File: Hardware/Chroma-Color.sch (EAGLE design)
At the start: 92 parts, among them J1 15-91-1102, J2 87832-6422, J3 1775470-6, J4 D2514-6V0C-AR-WD, J7 26-64-4040, U1 EP4CE6E22C8N, U2 ADP3338AKCZ-3.3-RL, U3 ADP3338AKCZ-2.5-RL, U4 NCV565ST12T3G, U5 M25P40-VMN6TPBCT, X1 ASDMB-50.000MHZ-LC-T

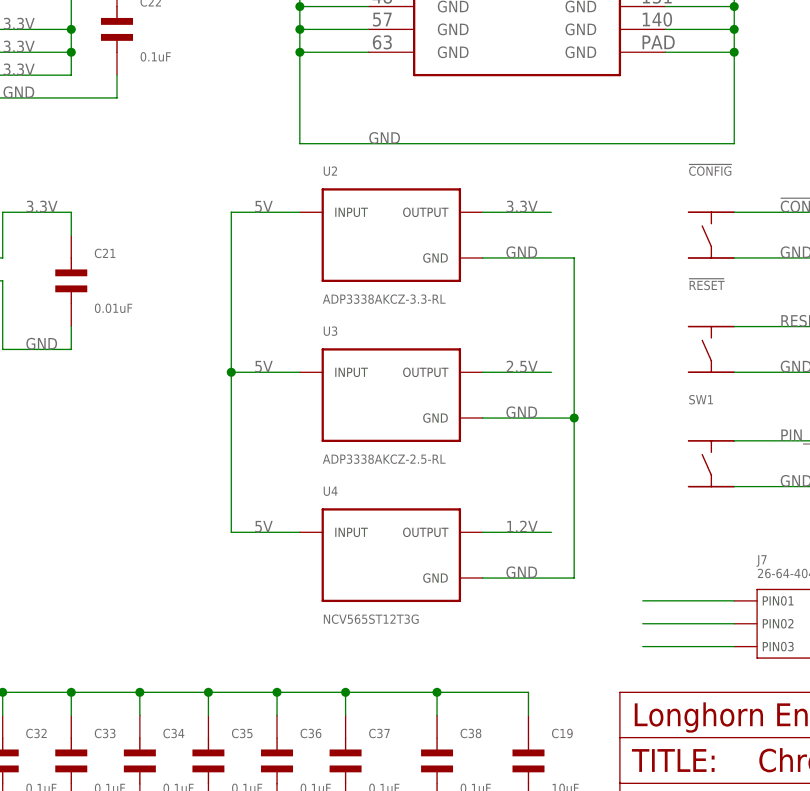
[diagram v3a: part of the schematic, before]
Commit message: Fixed voltage regulators to use newer library
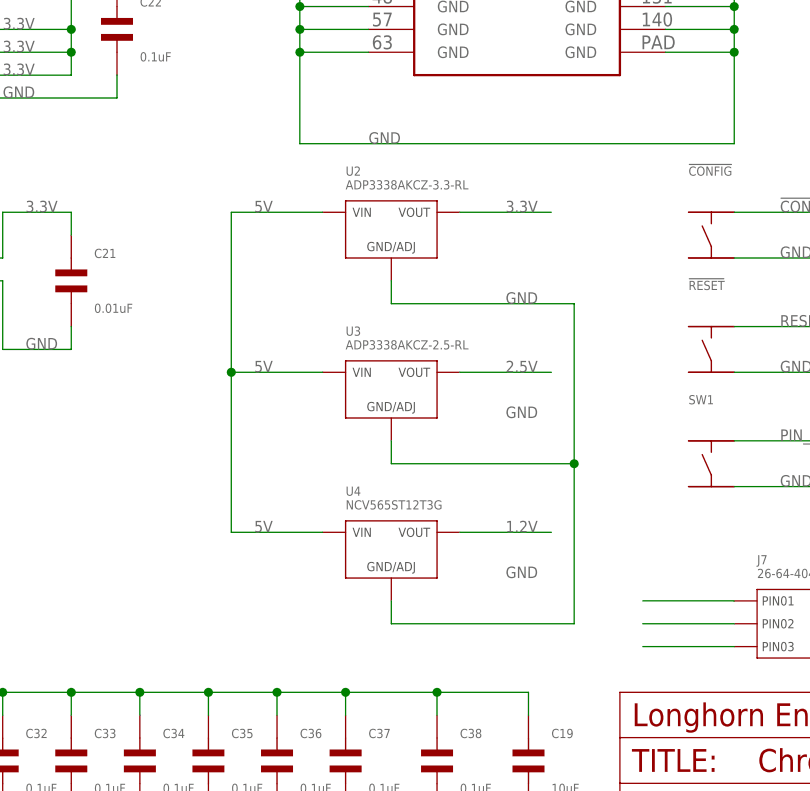
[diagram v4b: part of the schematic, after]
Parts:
- U2: device PP_PowerIC:ADP3338AKCZ-3.3-RL -> PP_PowerIC:LINEAR_VOTLAGE_REGULATORS_ADP3338
- U3: device PP_PowerIC:ADP3338AKCZ-2.5-RL -> PP_PowerIC:LINEAR_VOTLAGE_REGULATORS_ADP3338
- U4: device PP_PowerIC:NCV565ST12T3G -> PP_PowerIC:LINEAR_VOTLAGE_REGULATORS_NCV565ST12T3G
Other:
- moved on the sheet: U2, U3, U4

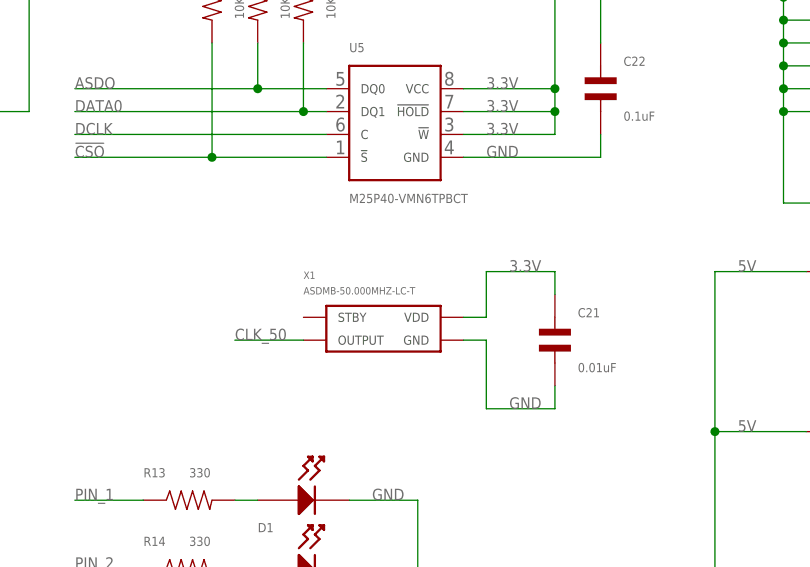
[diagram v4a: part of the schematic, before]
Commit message: Updated to latest library style.
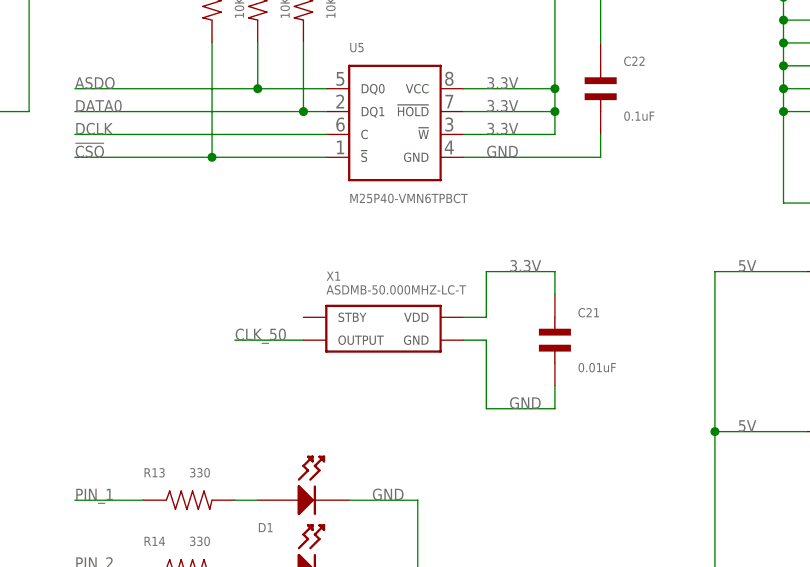
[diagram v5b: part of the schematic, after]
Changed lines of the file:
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@@
 <grid distance="0.1" unitdist="inch" unit="inch" style="lines" multiple="1" display="no" altdistance="0.01" altunitdist="inch" altunit="inch"/>
 <layers>
-<layer number="1" name="Top" color="14" fill="1" visible="yes" active="no"/>
-<layer number="2" name="Route2" color="12" fill="1" visible="yes" active="no"/>
-<layer number="3" name="Route3" color="4" fill="3" visible="yes" active="no"/>
-<layer number="4" name="Route4" color="1" fill="4" visible="yes" active="no"/>
-<layer number="5" name="Route5" color="4" fill="4" visible="yes" active="no"/>
-<layer number="6" name="Route6" color="1" fill="8" visible="yes" active="no"/>
-<layer number="7" name="Route7" color="4" fill="8" visible="yes" active="no"/>
-<layer number="8" name="Route8" color="1" fill="2" visible="yes" active="no"/>
-<layer number="9" name="Route9" color="4" fill="2" visible="yes" active="no"/>
-<layer number="10" name="Route10" color="1" fill="7" visible="yes" active="no"/>
-<layer number="11" name="Route11" color="4" fill="7" visible="yes" active="no"/>
-<layer number="12" name="Route12" color="1" fill="5" visible="yes" active="no"/>
-<layer number="13" name="Route13" color="4" fill="5" visible="yes" active="no"/>
-<layer number="14" name="Route14" color="1" fill="6" visible="yes" active="no"/>
-<layer number="15" name="Route15" color="9" fill="1" visible="yes" active="no"/>
-<layer number="16" name="Bottom" color="13" fill="1" visible="yes" active="no"/>
-<layer number="17" name="Pads" color="2" fill="1" visible="yes" active="no"/>
-<layer number="18" name="Vias" color="2" fill="1" visible="yes" active="no"/>
-<layer number="19" name="Unrouted" color="6" fill="1" visible="yes" active="no"/>
-<layer number="20" name="Dimension" color="15" fill="1" visible="yes" active="no"/>
-<layer number="21" name="tPlace" color="7" fill="1" visible="yes" active="no"/>
-<layer number="22" name="bPlace" color="7" fill="1" visible="yes" active="no"/>
-<layer number="23" name="tOrigins" color="15" fill="1" visible="yes" active="no"/>
-<layer number="24" name="bOrigins" color="15" fill="1" visible="yes" active="no"/>
-<layer number="25" name="tNames" color="7" fill="1" visible="yes" active="no"/>
-<layer number="26" name="bNames" color="7" fill="1" visible="yes" active="no"/>
-<layer number="27" name="tValues" color="7" fill="1" visible="yes" active="no"/>
-<layer number="28" name="bValues" color="7" fill="1" visible="yes" active="no"/>
+<layer number="1" name="Top" color="14" fill="1" visible="no" active="no"/>
+<layer number="2" name="Route2" color="12" fill="1" visible="no" active="no"/>
+<layer number="3" name="Route3" color="4" fill="3" visible="no" active="no"/>
+<layer number="4" name="Route4" color="1" fill="4" visible="no" active="no"/>
+<layer number="5" name="Route5" color="4" fill="4" visible="no" active="no"/>
+<layer number="6" name="Route6" color="1" fill="8" visible="no" active="no"/>
+<layer number="7" name="Route7" color="4" fill="8" visible="no" active="no"/>
+<layer number="8" name="Route8" color="1" fill="2" visible="no" active="no"/>
+<layer number="9" name="Route9" color="4" fill="2" visible="no" active="no"/>
+<layer number="10" name="Route10" color="1" fill="7" visible="no" active="no"/>
+<layer number="11" name="Route11" color="4" fill="7" visible="no" active="no"/>
+<layer number="12" name="Route12" color="1" fill="5" visible="no" active="no"/>
+<layer number="13" name="Route13" color="4" fill="5" visible="no" active="no"/>
+<layer number="14" name="Route14" color="1" fill="6" visible="no" active="no"/>
+<layer number="15" name="Route15" color="9" fill="1" visible="no" active="no"/>
+<layer number="16" name="Bottom" color="13" fill="1" visible="no" active="no"/>
+<layer number="17" name="Pads" color="2" fill="1" visible="no" active="no"/>
+<layer number="18" name="Vias" color="2" fill="1" visible="no" active="no"/>
+<layer number="19" name="Unrouted" color="6" fill="1" visible="no" active="no"/>
+<layer number="20" name="Dimension" color="15" fill="1" visible="no" active="no"/>
+<layer number="21" name="tPlace" color="7" fill="1" visible="no" active="no"/>
+<layer number="22" name="bPlace" color="7" fill="1" visible="no" active="no"/>
+<layer number="23" name="tOrigins" color="15" fill="1" visible="no" active="no"/>
+<layer number="24" name="bOrigins" color="15" fill="1" visible="no" active="no"/>
+<layer number="25" name="tNames" color="7" fill="1" visible="no" active="no"/>
+<layer number="26" name="bNames" color="7" fill="1" visible="no" active="no"/>
+<layer number="27" name="tValues" color="7" fill="1" visible="no" active="no"/>
+<layer number="28" name="bValues" color="7" fill="1" visible="no" active="no"/>
 <layer number="29" name="tStop" color="7" fill="3" visible="no" active="no"/>
 <layer number="30" name="bStop" color="7" fill="6" visible="no" active="no"/>
@@
 <layer number="35" name="tGlue" color="7" fill="4" visible="no" active="no"/>
 <layer number="36" name="bGlue" color="7" fill="5" visible="no" active="no"/>
-<layer number="37" name="tTest" color="7" fill="1" visible="yes" active="no"/>
-<layer number="38" name="bTest" color="7" fill="1" visible="yes" active="no"/>
+<layer number="37" name="tTest" color="7" fill="1" visible="no" active="no"/>
+<layer number="38" name="bTest" color="7" fill="1" visible="no" active="no"/>
 <layer number="39" name="tKeepout" color="4" fill="11" visible="no" active="no"/>
 <layer number="40" name="bKeepout" color="1" fill="11" visible="no" active="no"/>
@@
 <layer number="44" name="Drills" color="7" fill="1" visible="no" active="no"/>
 <layer number="45" name="Holes" color="7" fill="1" visible="no" active="no"/>
-<layer number="46" name="Milling" color="3" fill="1" visible="yes" active="no"/>
-<layer number="47" name="Measures" color="7" fill="1" visible="yes" active="no"/>
-<layer number="48" name="Document" color="7" fill="1" visible="yes" active="no"/>
-<layer number="49" name="Reference" color="7" fill="1" visible="yes" active="no"/>
-<layer number="50" name="dxf" color="7" fill="1" visible="yes" active="no"/>
-<layer number="51" name="tDocu" color="7" fill="1" visible="yes" active="no"/>
-<layer number="52" name="bDocu" color="7" fill="1" visible="yes" active="no"/>
-<layer number="53" name="tGND_GNDA" color="7" fill="9" visible="yes" active="no"/>
-<layer number="54" name="bGND_GNDA" color="1" fill="9" visible="yes" active="no"/>
-<layer number="56" name="wert" color="7" fill="1" visible="yes" active="no"/>
+<layer number="46" name="Milling" color="3" fill="1" visible="no" active="no"/>
+<layer number="47" name="Measures" color="7" fill="1" visible="no" active="no"/>
+<layer number="48" name="Document" color="7" fill="1" visible="no" active="no"/>
+<layer number="49" name="Reference" color="7" fill="1" visible="no" active="no"/>
+<layer number="50" name="dxf" color="7" fill="1" visible="no" active="no"/>
+<layer number="51" name="tDocu" color="7" fill="1" visible="no" active="no"/>
+<layer number="52" name="bDocu" color="7" fill="1" visible="no" active="no"/>
+<layer number="53" name="tGND_GNDA" color="7" fill="9" visible="no" active="no"/>
+<layer number="54" name="bGND_GNDA" color="1" fill="9" visible="no" active="no"/>
+<layer number="56" name="wert" color="7" fill="1" visible="no" active="no"/>
 <layer number="91" name="Nets" color="2" fill="1" visible="yes" active="yes"/>
 <layer number="92" name="Busses" color="1" fill="1" visible="yes" active="yes"/>
